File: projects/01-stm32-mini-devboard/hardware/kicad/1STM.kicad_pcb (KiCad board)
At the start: 2 copper layers, 6 parts, among them J1 USB_C_Receptacle_USB2.0_16P, U1 STM32F412CEUx

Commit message: Scheme power finish
Schemat:
-zakończono pracę nad sekcją zasilania
PCB:
-w rozstypce
Reszta:
-nic
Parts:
- added C2: 100nF, Capacitor_SMD:C_0603_1608Metric, F.Cu at (139.2, 87.1)
- added C3: 100nF, Capacitor_SMD:C_0603_1608Metric, F.Cu at (142.5, 77.2)
- added C4: 100nF, Capacitor_SMD:C_0603_1608Metric, F.Cu at (132.6, 74.8)
- added C5: 100nF, Capacitor_SMD:C_0603_1608Metric, F.Cu at (129.8, 82.3)
- added C6: 1u, Capacitor_SMD:C_0603_1608Metric, F.Cu at (152.2, 89.2)
- added C7: 1u, Capacitor_SMD:C_0603_1608Metric, F.Cu at (152.2, 91.7)
- added R4: 5K1, Resistor_SMD:R_0805_2012Metric, F.Cu at (148.0, 84.8)
- added R5: 5K1, Resistor_SMD:R_0805_2012Metric, F.Cu at (148.0, 87.7)
- added U2: AP2112K-3.3TRG1, Package_TO_SOT_SMD:SOT-23-5, F.Cu at (152.8, 85.7)
- moved U1 6.26 mm to (136.1, 81.0)
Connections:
- U1 pad 1: unconnected-(U1-VBAT-Pad1) -> Net-(U1-VBAT)
- U1 pad 13: /D+_USB -> unconnected-(U1-PA3-Pad13)
- U1 pad 14: /D-_USB -> unconnected-(U1-PA4-Pad14)
- U1 pad 24: unconnected-(U1-VDD-Pad24) -> Net-(U1-VBAT)
- U1 pad 32: unconnected-(U1-PA11-Pad32) -> /D-_USB
- U1 pad 33: unconnected-(U1-PA12-Pad33) -> /D+_USB
- U1 pad 34: unconnected-(U1-PA13-Pad34) -> /SWDIO
- U1 pad 36: unconnected-(U1-VDD-Pad36) -> Net-(C3-Pad1)
- U1 pad 37: unconnected-(U1-PA14-Pad37) -> /SWCLK
- U1 pad 44: unconnected-(U1-BOOT0-Pad44) -> Net-(U1-BOOT0)
- U1 pad 48: unconnected-(U1-VDD-Pad48) -> Net-(C4-Pad1)
- U1 pad 7: unconnected-(U1-NRST-Pad7) -> /NRST
- U1 pad 9: unconnected-(U1-VDDA-Pad9) -> Net-(U1-VDDA)
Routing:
- net Net-(C3-Pad1): track 0.00 -> 2.63 mm
- net Net-(C4-Pad1): track 0.00 -> 2.21 mm
- net Net-(U1-VDDA): track 0.00 -> 2.12 mm
- net Net-(U1-VBAT): track 0.00 -> 2.11 mm

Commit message: Added led's, switches general cleanup of nets
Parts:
- added C8: 100nF, Capacitor_SMD:C_0603_1608Metric, F.Cu at (111.2, 105.2)
- added D1: BLUE_LED, LED_SMD:LED_1206_3216Metric, F.Cu at (121.8, 98.9)
- added D2: RED_LED, LED_SMD:LED_1206_3216Metric, F.Cu at (121.8, 102.3)
- added R3: 5K1, Resistor_SMD:R_0805_2012Metric, F.Cu at (121.2, 89.9)
- added R6: 5K1, Resistor_SMD:R_0805_2012Metric, F.Cu at (121.2, 92.8)
- added R7: 330, Resistor_SMD:R_0805_2012Metric, F.Cu at (121.2, 95.8)
- added SW1: B3F-1002, Button_Switch_THT:SW_TH_Tactile_Omron_B3F-100x, F.Cu at (110.9, 90.0)
- added SW2: B3F-1002, Button_Switch_THT:SW_TH_Tactile_Omron_B3F-100x, F.Cu at (110.9, 97.8)
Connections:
- net /D-_USB renamed D-_USB
- C7 pad 2: +3.3V -> D+_USB
- J1 pad A6: /D+_USB -> D+_USB
- J1 pad B6: /D+_USB -> D+_USB
- U1 pad 14: unconnected-(U1-PA4-Pad14) -> /SPI1_NSS
- U1 pad 15: unconnected-(U1-PA5-Pad15) -> /SPI1_SCK
- U1 pad 16: unconnected-(U1-PA6-Pad16) -> SPI1_MISO
- U1 pad 17: unconnected-(U1-PA7-Pad17) -> SPI1_MOSI
- U1 pad 2: unconnected-(U1-PC13-Pad2) -> /GPIO (IRQ)
- U1 pad 21: unconnected-(U1-PB10-Pad21) -> /I2S2_CK
- U1 pad 28: unconnected-(U1-PB15-Pad28) -> /I2S2_SD
- U1 pad 3: unconnected-(U1-PC14-Pad3) -> /GPIO (CE)
- U1 pad 33: /D+_USB -> D+_USB
- U1 pad 38: unconnected-(U1-PA15-Pad38) -> I2S3_WS
- U1 pad 39: unconnected-(U1-PB3-Pad39) -> /I2S3_CK
- U1 pad 41: unconnected-(U1-PB5-Pad41) -> /I2S3_SD
- U1 pad 46: unconnected-(U1-PB9-Pad46) -> /I2S2_WS
- U1 pad 7: /NRST -> NRST
- U2 pad 1: unconnected-(U2-NC-Pad1) -> +5V
- U2 pad 4: +5V -> unconnected-(U2-NC-Pad4)
- U2 pad 5: +3.3V -> D+_USB
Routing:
- net D+_USB: track 0.00 -> 5.86 mm, vias 0 -> 1
- net /D+_USB: track 5.86 -> 0.00 mm, vias 1 -> 0

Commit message: Minor changes in schematic - still not make any changes to pcb
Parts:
- added J2: SWD 5P, Connector_PinHeader_2.54mm:PinHeader_1x05_P2.54mm_Vertical, F.Cu at (121.9, 77.7)
- added J3: SPI1, Connector_PinHeader_2.54mm:PinHeader_1x04_P2.54mm_Vertical, F.Cu at (121.9, 108.2)
- added J4: WE I2S2, Connector_PinHeader_2.54mm:PinHeader_1x03_P2.54mm_Vertical, F.Cu at (155.4, 110.2)
- added J5: WY I2S3, Connector_PinHeader_2.54mm:PinHeader_1x03_P2.54mm_Vertical, F.Cu at (155.4, 77.2)
- added J6: GPIO, Connector_PinHeader_2.54mm:PinHeader_1x02_P2.54mm_Vertical, F.Cu at (121.9, 96.5)
- moved SW1 37.7 mm to (142.2, 69.1)
- moved SW2 37.7 mm to (142.2, 76.8)
- moved C8 37.7 mm to (142.6, 84.2)
- moved R3 21.0 mm to (132.1, 71.9)
- moved R6 21.0 mm to (132.1, 74.8)
- moved R7 21.0 mm to (132.1, 77.8)
- moved D1 21.0 mm to (132.7, 80.9)
- moved D2 21.0 mm to (132.7, 84.3)
- moved C1 18.6 mm to (143.3, 111.5)
- moved C3 18.6 mm to (144.2, 95.7)
- moved C4 18.6 mm to (134.3, 93.3)
- moved J1 18.6 mm to (138.7, 126.5)
- moved R1 18.6 mm to (138.7, 112.0)
- moved R2 18.6 mm to (138.7, 116.5)
- moved R3 18.6 mm to (134.3, 114.9)
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
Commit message: Resistors optimalization
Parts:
- added C10: 30pF, Capacitor_SMD:C_0805_2012Metric, F.Cu at (166.2, 97.7)
- added C9: 30pF, Capacitor_SMD:C_0805_2012Metric, F.Cu at (166.2, 94.6)
- added R5: 10K, Resistor_SMD:R_0805_2012Metric, F.Cu at (161.7, 89.4)
- added R8: 65, Resistor_SMD:R_0805_2012Metric, F.Cu at (161.7, 92.3)
- added R9: 65, Resistor_SMD:R_0805_2012Metric, F.Cu at (161.7, 95.3)
- added Y1: 8MHz, Crystal:Crystal_SMD_5032-2Pin_5.0x3.2mm, F.Cu at (167.6, 90.5)
- D1: value BLUE_LED -> AMBER_LED
- R4: value 5K1 -> 10K
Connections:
- C2 pad 1: Net-(U1-VBAT) -> +3.3V
- C3 pad 1: Net-(C3-Pad1) -> +3.3V
- C4 pad 1: Net-(C4-Pad1) -> +3.3V
- C5 pad 1: Net-(U1-VDDA) -> +3.3V
- C7 pad 2: D+_USB -> +3.3V
- D1 pad 1: unconnected-(D1-K-Pad1) -> Net-(D1-K)
- D1 pad 2: D+_USB -> +3.3V
- D2 pad 1: GND -> Net-(D2-K)
- D2 pad 2: D+_USB -> +3.3V
- J2 pad 1: D+_USB -> +3.3V
- R4 pad 1: Net-(R4-Pad1) -> GND
- R7 pad 1: unconnected-(R7-Pad1) -> USR_SW
- U1 pad 1: Net-(U1-VBAT) -> +3.3V
- U1 pad 23: Net-(U1-VSS-Pad23) -> GND
- U1 pad 24: Net-(U1-VBAT) -> +3.3V
- U1 pad 29: unconnected-(U1-PA8-Pad29) -> USR_LED
- U1 pad 30: unconnected-(U1-PA9-Pad30) -> USR_SW
- U1 pad 35: Net-(U1-VSS-Pad23) -> GND
- U1 pad 36: Net-(C3-Pad1) -> +3.3V
- U1 pad 47: Net-(U1-VSS-Pad23) -> GND
- U1 pad 48: Net-(C4-Pad1) -> +3.3V
- U1 pad 49: Net-(U1-VSS-Pad23) -> GND
- U1 pad 5: unconnected-(U1-PH0-Pad5) -> OSC_IN
- U1 pad 6: unconnected-(U1-PH1-Pad6) -> OSC_OUT
- U1 pad 8: unconnected-(U1-VSSA-Pad8) -> GND
- U1 pad 9: Net-(U1-VDDA) -> +3.3V
- U2 pad 5: D+_USB -> +3.3V
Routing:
- net +3.3V: track 0.00 -> 9.07 mm
- net Net-(C3-Pad1): track 2.63 -> 0.00 mm
- net Net-(C4-Pad1): track 2.21 -> 0.00 mm
- net Net-(U1-VDDA): track 2.12 -> 0.00 mm
- net Net-(U1-VBAT): track 2.11 -> 0.00 mm

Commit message: PCB layout first steps
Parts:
- removed R3: 1K5, Resistor_SMD:R_0805_2012Metric
- removed R3, R6: 5K1, Resistor_SMD:R_0805_2012Metric
- removed the R5 at (148.8, 96.4)
- moved R9 51.7 mm to (119.9, 125.6), turned to -90 degrees
- moved R8 50.6 mm to (123.7, 125.7), turned to -90 degrees
- moved Y1 43.4 mm to (131.9, 115.2), turned to 90 degrees
- moved D1 41.8 mm to (119.9, 120.7), turned to 90 degrees
- moved R7 40.0 mm to (156.1, 109.7)
- moved SW2 39.5 mm to (167.2, 107.5), turned to 180 degrees
- moved C9 38.3 mm to (135.2, 117.2), turned to -90 degrees
- moved SW1 37.9 mm to (124.8, 102.8)
- moved D2 37.5 mm to (123.7, 120.7), turned to 90 degrees
- moved J6 35.9 mm to (129.4, 131.6), turned to 90 degrees
- moved C10 34.7 mm to (135.2, 113.3), turned to -90 degrees
- moved J2 34.4 mm to (145.4, 102.8), turned to -90 degrees
- moved R5 33.1 mm to (136.1, 110.3)
- moved J3 33.0 mm to (145.4, 131.4), turned to -90 degrees
- moved U2 32.3 mm to (162.1, 125.5), turned to 180 degrees
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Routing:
- net /SWCLK: track 0.00 -> 37.6 mm
- net /SWDIO: track 0.00 -> 36.3 mm
- net +5V: track 0.00 -> 20.9 mm
- net I2S3_WS: track 0.00 -> 19.3 mm
- net +3.3V: track 9.07 -> 25.0 mm
- net /I2S3_SD: track 0.00 -> 13.2 mm
- net /I2S3_CK: track 0.00 -> 13.2 mm
- net OSC_IN: track 0.00 -> 12.9 mm
- net OSC_OUT: track 0.00 -> 12.5 mm
- net NRST: track 0.00 -> 11.5 mm
- net Net-(R7-Pad2): track 0.00 -> 11.1 mm
- net D+_USB: track 5.86 -> 0.00 mm, vias 1 -> 0
- net D-_USB: track 5.26 -> 0.00 mm, vias 1 -> 0
- net Net-(U1-VCAP_1): track 0.00 -> 3.51 mm
- net Net-(J1-CC1): track 7.90 -> 4.51 mm
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
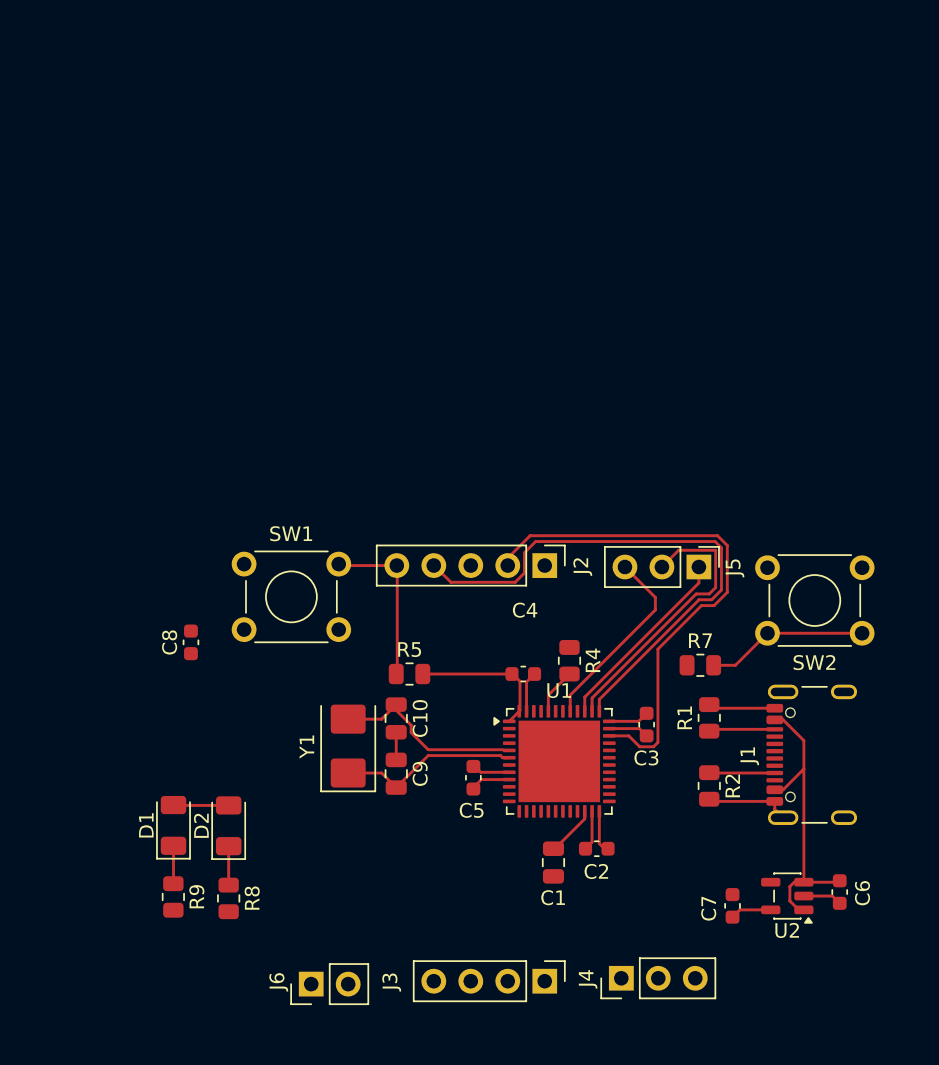
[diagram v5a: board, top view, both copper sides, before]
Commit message: PCB Layout v1
Finished first pcb layout attempt routings to be optimized especially routings of power delivery.
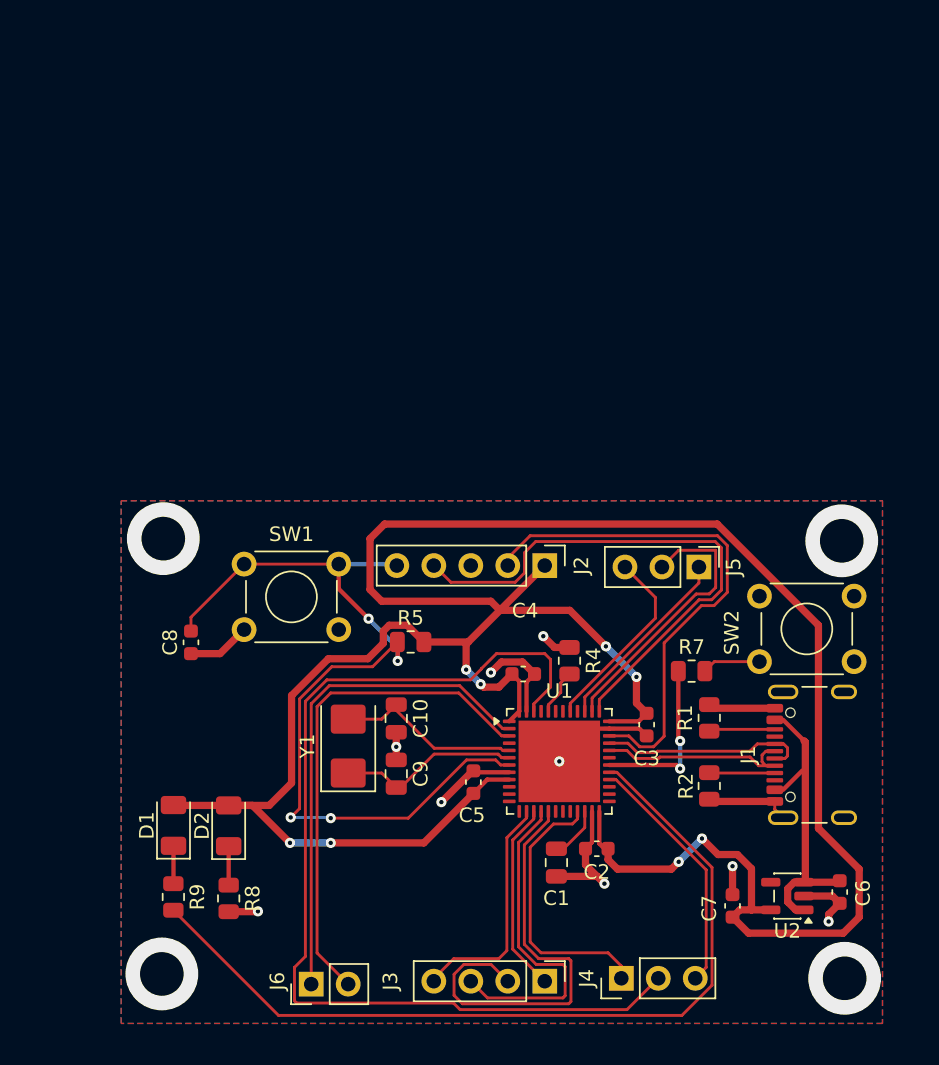
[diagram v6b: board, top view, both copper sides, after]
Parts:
- moved R5 2.20 mm to (136.2, 108.1)
- moved SW2 2.03 mm to (166.7, 109.5)
- moved R7 0.72 mm to (155.5, 110.1)
- moved C5 0.30 mm to (140.5, 117.7)
- moved C1 0.20 mm to (146.2, 123.2)
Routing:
- net +3.3V: track 25.0 -> 185.7 mm, vias 0 -> 8
- net /I2S2_WS: track 0.00 -> 69.4 mm
- net USR_LED: track 0.00 -> 58.7 mm
- net NRST: track 11.5 -> 60.0 mm, vias 0 -> 4
- net /GPIO (CE): track 0.00 -> 34.8 mm
- net /GPIO (IRQ): track 0.00 -> 34.6 mm
- net SPI1_MOSI: track 0.00 -> 30.5 mm
- net GND: track 25.5 -> 54.3 mm, vias 0 -> 9
- net SPI1_MISO: track 0.00 -> 22.7 mm
- net /I2S2_CK: track 0.00 -> 18.9 mm
- net /I2S2_SD: track 0.00 -> 17.0 mm
- net /SPI1_NSS: track 0.00 -> 16.1 mm
- net D+_USB: track 0.00 -> 14.4 mm
- net D-_USB: track 0.00 -> 14.3 mm
- net /SPI1_SCK: track 0.00 -> 13.2 mm
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- added copper zone on B.Cu, net GND
- added copper zone on F.Cu, net GND

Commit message: Dodano edge cuts
-Edgecuts
-minor gnd plane adjustments
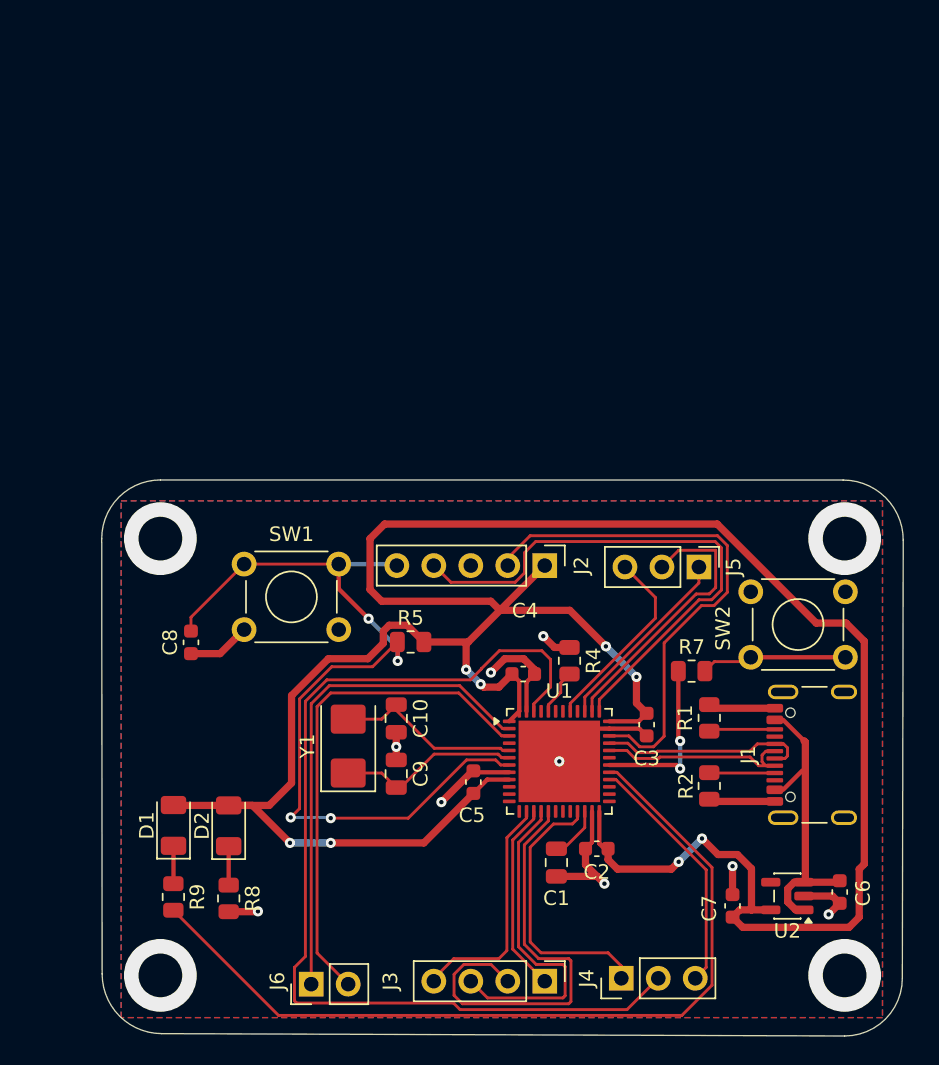
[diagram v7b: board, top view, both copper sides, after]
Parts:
- moved SW2 0.67 mm to (166.1, 109.2)
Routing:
- net Net-(R7-Pad2): track 4.02 -> 10.5 mm
- net GND: track 54.3 -> 52.8 mm
- net +3.3V: track 185.7 -> 186.8 mm
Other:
- board outline added: 55.1 x 38.2 mm
